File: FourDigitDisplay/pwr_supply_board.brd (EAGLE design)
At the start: 65 x 47 mm, 28 parts, among them CN1 POWER_IF, CN2 POWER_IF, CN3 POWER_IF, Q1 2SA1020L-Y, Q2 2SK3234, U1 MC34063AP1, U5 XC6202P502TB

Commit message: 電源基板の部品配線
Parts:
- C1: device Parts:ELECAP_200MIL -> Parts:ELECAP_100MIL
- moved CN2 60.7 mm to (3.81, 12.7), turned to 270 degrees
- moved R7 21.9 mm to (25.1, 3.17), turned to 0 degrees
- moved R6 19.4 mm to (44.8, 3.17), turned to 0 degrees
- moved CN3 17.7 mm to (3.81, 20.3), turned to 270 degrees
- moved R2 10.8 mm to (17.1, 32.4), turned to 0 degrees
- moved C6 10.0 mm to (13.3, 5.71), turned to 270 degrees
- moved C2 8.08 mm to (15.9, 15.9)
- moved U1 7.65 mm to (13.3, 24.1)
- moved CN1 7.62 mm to (3.81, 27.9)
- moved C1 7.18 mm to (3.81, 33.0)
- moved R1 6.54 mm to (17.1, 42.5)
- moved R3 6.54 mm to (17.1, 37.5)
- moved C5 5.46 mm to (8.26, 5.71), turned to 270 degrees
- moved Q2 4.07 mm to (26.0, 26.7), turned to 180 degrees
- moved U5 4.07 mm to (8.26, 11.4), turned to 0 degrees
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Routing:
- net +24V: track 0.00 -> 93.7 mm
- net +12V: track 0.00 -> 58.5 mm
- net N$6: track 0.00 -> 52.8 mm
- net N$2: track 0.00 -> 36.5 mm
- net N$5: track 0.00 -> 32.0 mm
- net N$10: track 0.00 -> 25.2 mm
- net N$7: track 0.00 -> 24.6 mm
- net N$4: track 0.00 -> 13.4 mm
- net +5V: track 0.00 -> 12.6 mm
- net N$8: track 0.00 -> 12.1 mm
- net N$1: track 0.00 -> 11.4 mm
- net N$9: track 0.00 -> 4.45 mm
- net N$3: track 0.00 -> 4.45 mm
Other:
- board size 65 x 47 mm -> 62 x 45 mm

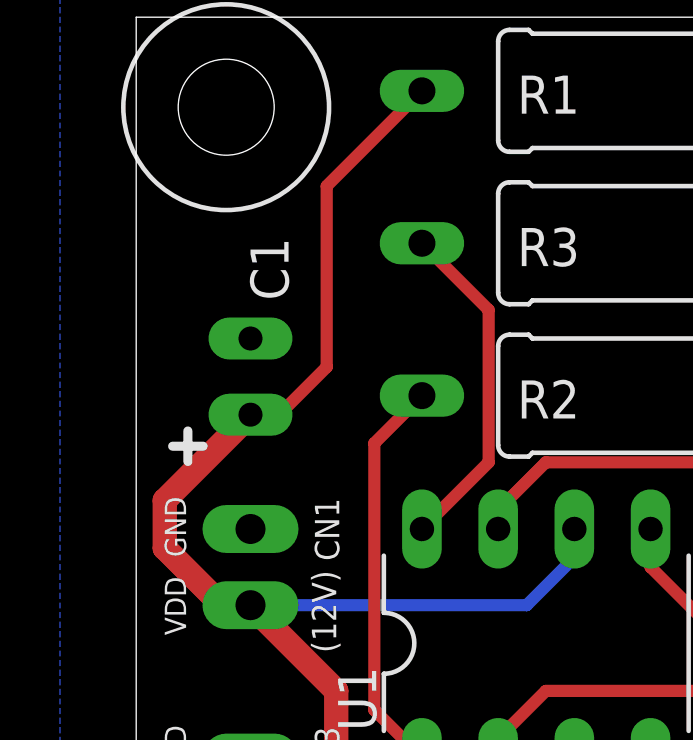
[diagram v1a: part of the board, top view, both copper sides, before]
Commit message: 配線を一部修正
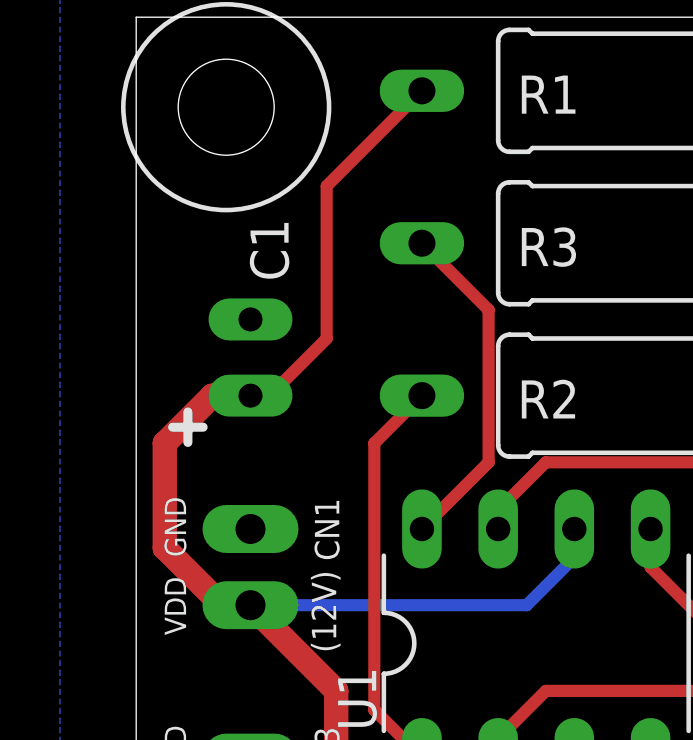
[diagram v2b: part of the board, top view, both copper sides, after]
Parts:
- moved C1 0.63 mm to (3.81, 33.7)
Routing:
- net +12V: track 58.5 -> 59.1 mm
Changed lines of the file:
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@@
 <setting verticaltext="up"/>
 </settings>
-<grid distance="25" unitdist="mil" unit="mil" style="lines" multiple="1" display="yes" altdistance="0.025" altunitdist="inch" altunit="inch"/>
+<grid distance="12.5" unitdist="mil" unit="mil" style="lines" multiple="1" display="yes" altdistance="0.025" altunitdist="inch" altunit="inch"/>
 <layers>
 <layer number="1" name="Top" color="4" fill="1" visible="yes" active="yes"/>
@@
 </autorouter>
 <elements>
-<element name="C1" library="Parts" package="ELECAP_100MIL" value="100uF/16V" x="3.81" y="33.02" smashed="yes" rot="R90">
-<attribute name="NAME" x="5.08" y="35.56" size="1.27" layer="25" ratio="10" rot="R90"/>
-<attribute name="VALUE" x="7.493" y="33.655" size="1.27" layer="27" ratio="10" rot="R90"/>
+<element name="C1" library="Parts" package="ELECAP_100MIL" value="100uF/16V" x="3.81" y="33.655" smashed="yes" rot="R90">
+<attribute name="NAME" x="5.08" y="36.195" size="1.27" layer="25" ratio="10" rot="R90"/>
+<attribute name="VALUE" x="7.493" y="34.29" size="1.27" layer="27" ratio="10" rot="R90"/>
 </element>
 <element name="C2" library="Parts" package="CAP_100MIL" value="1500pF" x="15.875" y="15.875" smashed="yes">
@@
 <wire x1="3.81" y1="25.4" x2="2.8575" y2="25.4" width="0.8128" layer="1"/>
 <wire x1="2.8575" y1="25.4" x2="0.9525" y2="27.305" width="0.8128" layer="1"/>
-<wire x1="0.9525" y1="27.305" x2="0.9525" y2="28.8925" width="0.8128" layer="1"/>
-<wire x1="0.9525" y1="28.8925" x2="3.81" y2="31.75" width="0.8128" layer="1"/>
-<wire x1="3.81" y1="31.75" x2="4.7625" y2="31.75" width="0.4064" layer="1"/>
-<wire x1="4.7625" y1="31.75" x2="6.35" y2="33.3375" width="0.4064" layer="1"/>
-<wire x1="6.35" y1="33.3375" x2="6.35" y2="39.37" width="0.4064" layer="1"/>
 <wire x1="6.35" y1="39.37" x2="9.525" y2="42.545" width="0.4064" layer="1"/>
 <wire x1="14.605" y1="27.94" x2="14.605" y2="26.9875" width="0.4064" layer="16"/>
 <wire x1="14.605" y1="26.9875" x2="13.0175" y2="25.4" width="0.4064" layer="16"/>
 <wire x1="13.0175" y1="25.4" x2="3.81" y2="25.4" width="0.4064" layer="16"/>
+<wire x1="6.35" y1="39.37" x2="6.35" y2="34.29" width="0.4064" layer="1"/>
+<wire x1="6.35" y1="34.29" x2="4.445" y2="32.385" width="0.4064" layer="1"/>
+<wire x1="4.445" y1="32.385" x2="3.81" y2="32.385" width="0.4064" layer="1"/>
+<wire x1="0.9525" y1="27.305" x2="0.9525" y2="30.7975" width="0.8128" layer="1"/>
+<wire x1="0.9525" y1="30.7975" x2="2.54" y2="32.385" width="0.8128" layer="1"/>
+<wire x1="2.54" y1="32.385" x2="3.81" y2="32.385" width="0.8128" layer="1"/>
 </signal>
 <signal name="0V">
